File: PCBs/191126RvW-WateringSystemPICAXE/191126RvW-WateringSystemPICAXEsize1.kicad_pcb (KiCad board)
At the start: 2 copper layers, 83.8 x 101.6 mm, 17 parts, among them J1 MotorConn, J2 SerIn, J3 SerSelect, J4 SerOut, J5 Screw_Terminal_01x04, J6 SerSelect, Q1 KN2222A, U1 PICAXEM2

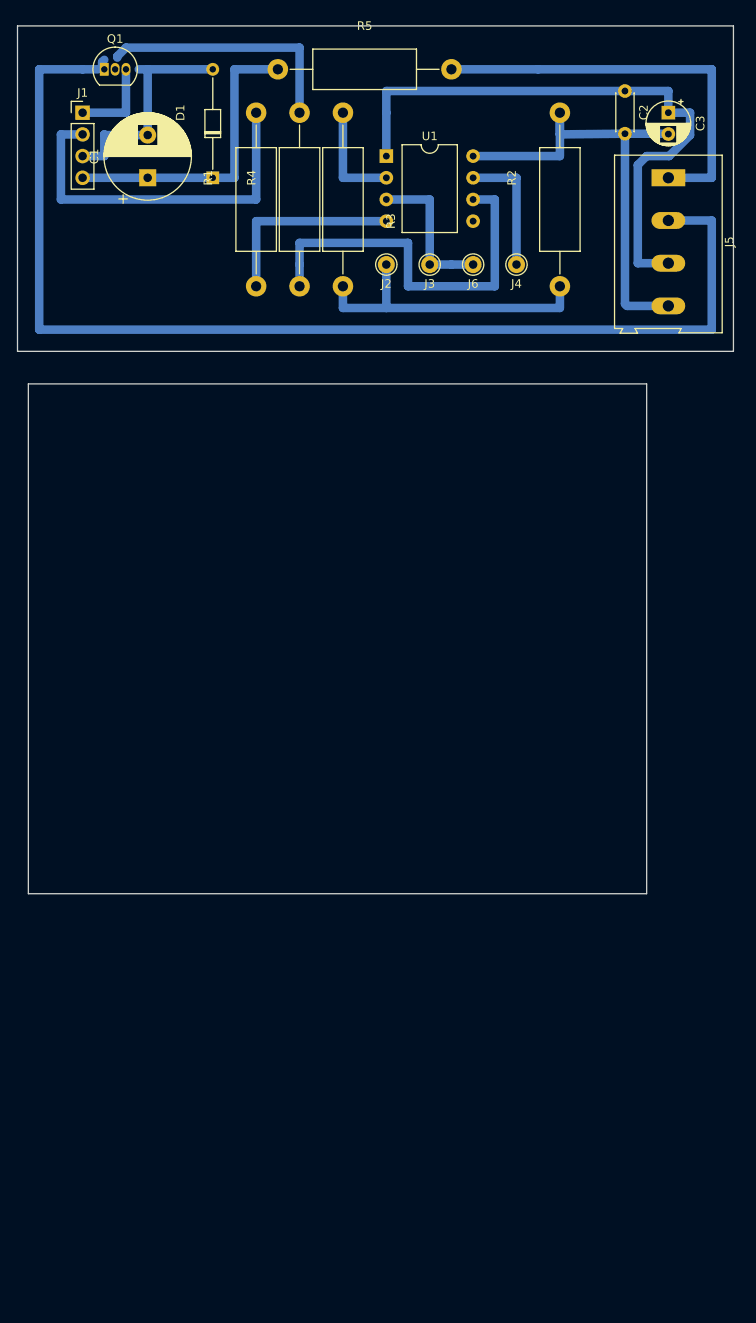
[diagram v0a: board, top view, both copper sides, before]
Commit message: Resized board to fit housing
Small housing
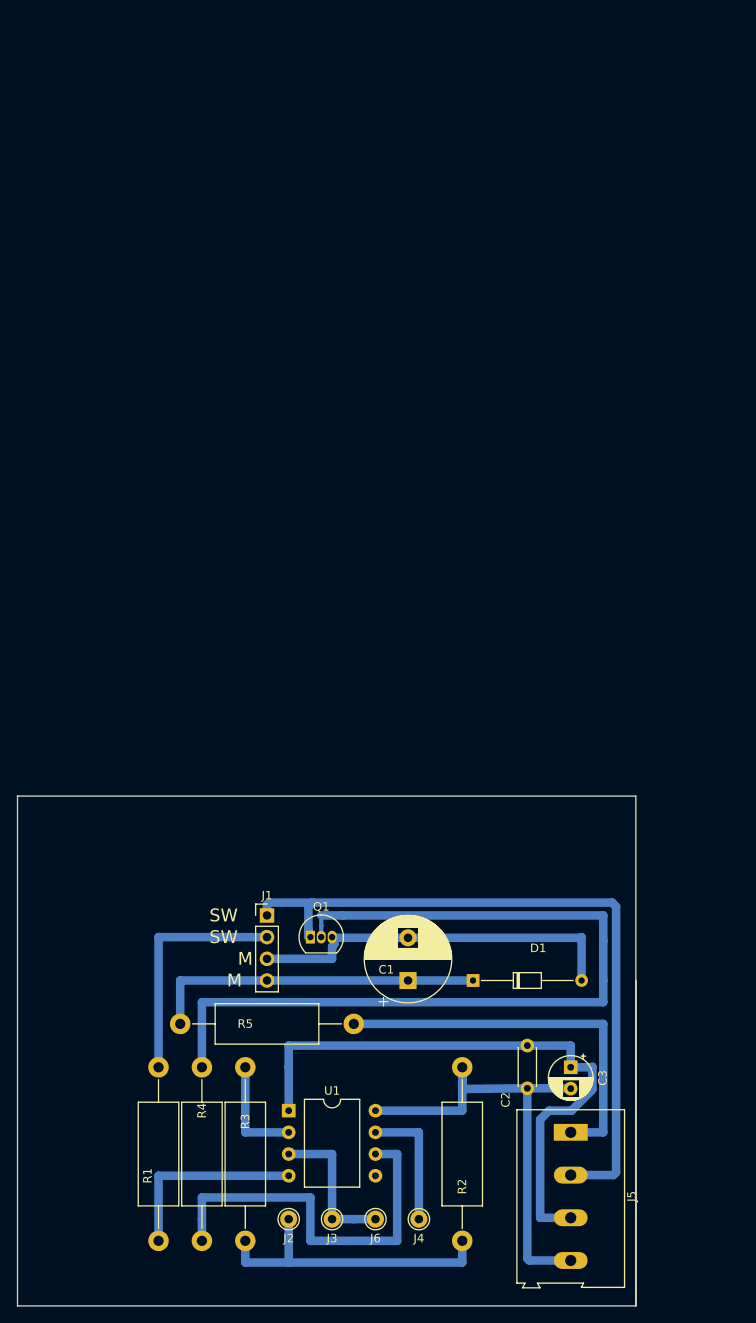
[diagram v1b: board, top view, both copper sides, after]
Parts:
- moved R1 112.3 mm to (85.1, 160.0)
- moved R2 112.3 mm to (120.7, 160.0)
- moved R4 112.3 mm to (90.2, 160.0)
- moved R5 112.3 mm to (87.6, 134.6)
- moved C2 112.3 mm to (128.3, 137.2)
- moved C3 112.3 mm to (133.3, 139.7)
- moved J2 112.3 mm to (100.3, 157.5)
- moved J3 112.3 mm to (105.4, 157.5)
- moved J4 112.3 mm to (115.6, 157.5)
- moved J5 112.3 mm to (133.3, 147.3)
- moved J6 112.3 mm to (110.5, 157.5)
- moved R3 112.3 mm to (95.2, 139.7)
- moved U1 112.3 mm to (100.3, 144.8)
- moved Q1 104.4 mm to (102.9, 124.5)
- moved C1 98.8 mm to (114.3, 129.5)
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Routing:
- net Net-(Q1-Pad2): track 29.5 -> 99.6 mm
- net GNDPWR: track 145.3 -> 83.2 mm
- net Net-(C1-Pad2): track 26.6 -> 44.4 mm
- net Net-(J1-Pad2): track 43.2 -> 27.9 mm
- net Net-(C1-Pad1): track 35.6 -> 39.4 mm
- net +5C: track 48.3 -> 45.7 mm
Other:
- board size 83.8 x 101.6 mm -> 72.4 x 59.7 mm
- board text added: "M"
- board text added: "SW"

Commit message: pcb changes
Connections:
- J1 pad 1: GNDPWR -> GNDD
- J5 pad 2: GNDPWR -> GNDD
- Q1 pad 1: GNDPWR -> GNDD
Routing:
- net GNDD: track 55.5 -> 154.0 mm
- net GNDPWR: track 83.2 -> 0.00 mm
